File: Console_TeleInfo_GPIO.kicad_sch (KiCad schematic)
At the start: 6 parts, among them J13 Conn_02x06_Odd_Even

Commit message: Finalize the schema
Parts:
- removed Conso, Pompe: Grove Serial, symbol BananaPI:Grove_Serial
- removed GPIO-8: Grove GPIO, symbol BananaPI:Grove_GPIO
- removed Tension: Jumper_3_Bridged12, symbol Jumper:Jumper_3_Bridged12
- added J1: UART7, symbol BananaPI:Grove_Serial
- added J10, J11, J12, J14, J15, J16, J21, J22, J23, J24: Grove I2C, symbol BananaPI:Grove_I2C
- added J17, J2: Grove Serial, symbol BananaPI:Grove_Serial
- added J18, J19, J3: Grove GPIO, symbol BananaPI:Grove_GPIO
- added J20: CAN, symbol BananaPI:Grove_Serial
- added J25: UART3, symbol BananaPI:Grove_Serial
- added J26: SPI, symbol Connector_Generic:Conn_02x05_Odd_Even
- added J9: CON3, symbol BananaPI:CON3
- added Tension1, Tension2, Tension3: Jumper_3_Bridged12, symbol Jumper:Jumper_3_Bridged12
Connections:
- net at Console.1 (GND), J13.8 (GND): now also J1.1 (GND)
- net at Console.2 (VCC), J13.2 (3.3V): now also J1.2 (VCC), J2.2 (VCC), Tension1.1 (A)
- net at J13.1 (5V): now also Tension1.3 (B)
- net at J13.3 (RX4): now also J2.4 (RX)
- net at J13.4 (RX7): now also J1.4 (RX)
- net at J13.5 (IO-8): now also J3.4 (GP0)
- net at J13.6 (TX7): now also J1.3 (TX)
- net at J13.7 (GND): now also J2.1 (GND), J3.1 (GND)
- new net: J10.1 (GND), J11.1 (GND), J12.1 (GND), J14.1 (GND), J15.1 (GND), J16.1 (GND), J17.1 (GND), J18.1 (GND), J19.1 (GND), J20.1 (GND), J21.1 (GND), J22.1 (GND), J23.1 (GND), J24.1 (GND), J25.1 (GND), J26.2 (Pin_2), J9.14 (GND), J9.20 (GND), J9.6 (GND), J9.9 (GND)
- new net: J16.2 (VCC), J17.2 (VCC), J20.2 (VCC), J21.2 (VCC), J22.2 (VCC), J23.2 (VCC), J24.2 (VCC), J25.2 (VCC), J26.9 (Pin_9), J9.1 (3.3v), J9.17 (3.3v), Tension2.1 (A), Tension3.1 (A)
- new net: J20.3 (TX), J9.16 (CAN_TX)
- new net: J20.4 (RX), J9.18 (CAN_RX)
- new net: J26.1 (Pin_1), J9.24 (CS0)
- new net: J26.10 (Pin_10), J9.23 (SPICLK)
- new net: J26.3 (Pin_3), J9.26 (CS1)
- new net: J26.5 (Pin_5), J9.21 (MISO)
- new net: J26.7 (Pin_7), J9.19 (MOSI)
- new net: J10.3 (SDA), J11.3 (SDA), J12.3 (SDA), J14.3 (SDA), J15.3 (SDA), J16.3 (SDA), J21.3 (SDA), J22.3 (SDA), J23.3 (SDA), J24.3 (SDA), J9.3 (SDA)
- new net: J10.4 (SCL), J11.4 (SCL), J12.4 (SCL), J14.4 (SCL), J15.4 (SCL), J16.4 (SCL), J21.4 (SCL), J22.4 (SCL), J23.4 (SCL), J24.4 (SCL), J9.5 (SCK)
- new net: J19.2 (VCC), Tension3.2 (C)
- new net: J19.3 (GP1), J9.12 (IO_1)
- new net: J19.4 (GP0), J9.7 (PWM)
- new net: J10.2 (VCC), J11.2 (VCC), J12.2 (VCC), J14.2 (VCC), J15.2 (VCC), J9.2 (5v), J9.4 (5V), Tension2.3 (B), Tension3.3 (B)
- new net: J18.2 (VCC), Tension2.2 (C)
- new net: J18.3 (GP1), J9.22 (RTS2)
- new net: J18.4 (GP0), J9.15 (CTS2)
- new net: J25.3 (TX), J9.8 (TX3)
- new net: J25.4 (RX), J9.10 (RX3)
- new net: J3.2 (VCC), Tension1.2 (C)
- new net: J17.4 (RX), J9.11 (RX2)
- new net: J17.3 (TX), J9.13 (TX2)
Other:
- moved on the sheet: Console, J13

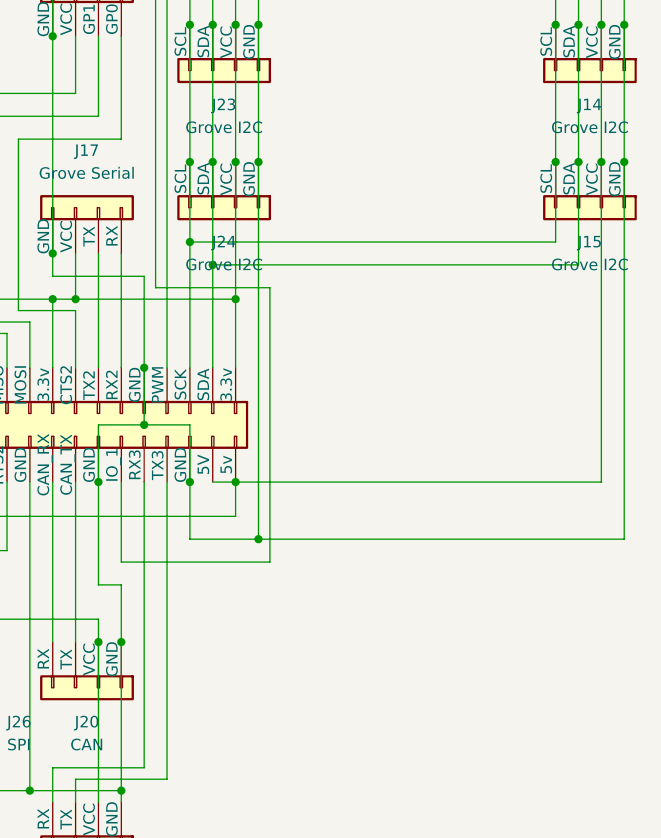
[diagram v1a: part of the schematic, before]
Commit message: Add level shifter
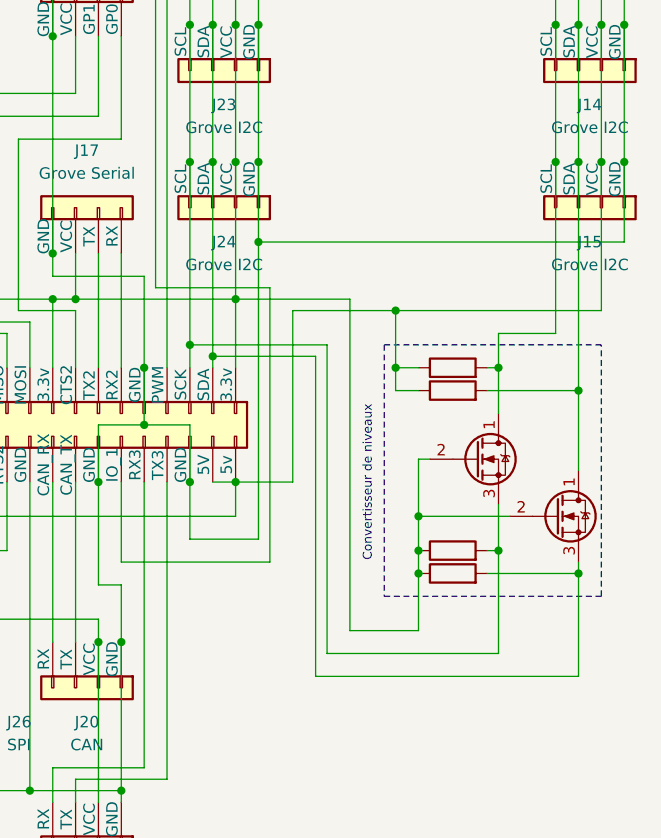
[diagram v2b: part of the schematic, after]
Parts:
- added Q1, Q2: Q_NMOS_DGS, symbol Device:Q_NMOS_DGS
- added R1, R2, R3, R4: R, symbol Device:R
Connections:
- net at J16.2 (VCC), J17.2 (VCC), J20.2 (VCC)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: now also Q1.2 (G), Q2.2 (G), R1.1, R2.1
- net at J16.3 (SDA), J21.3 (SDA), J22.3 (SDA)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: now also Q1.3 (S), R1.2; no longer J10.3 (SDA), J11.3 (SDA), J12.3 (SDA), J14.3 (SDA), J15.3 (SDA)
- net at J16.4 (SCL), J21.4 (SCL), J22.4 (SCL)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: now also Q2.3 (S), R2.2; no longer J10.4 (SCL), J11.4 (SCL), J12.4 (SCL), J14.4 (SCL), J15.4 (SCL)
- net at J10.2 (VCC), J11.2 (VCC), J12.2 (VCC)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: now also R3.1, R4.1
- new net: J10.3 (SDA), J11.3 (SDA), J12.3 (SDA), J14.3 (SDA), J15.3 (SDA), Q1.1 (D), R3.2
- new net: J10.4 (SCL), J11.4 (SCL), J12.4 (SCL), J14.4 (SCL), J15.4 (SCL), Q2.1 (D), R4.2
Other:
- note added: "Convertisseur de niveaux"

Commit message: Renew console + Linky
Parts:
- added J4: Conn_02x06_Odd_Even, symbol BananaPI:J11
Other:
- moved on the sheet: Console, J1, J13, J2, J3, Tension1
